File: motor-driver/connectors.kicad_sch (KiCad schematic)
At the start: 2 parts, among them J3 XT60PW-F, J4 B2B-PH-SM4-TB

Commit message: post revisions
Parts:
- added J1: USB_B_Micro, Connector_USB:USB_Micro-B_Amphenol_10103594-0001LF_Horizontal, symbol Connector:USB_B_Micro
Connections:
- net 5V: now also J1.1 (VBUS)
- net GND: now also J1.5 (GND), J1.6 (Shield)
- net 14V renamed V_BUS
- new net USB_D+: J1.3 (D+)
- new net USB_D-: J1.2 (D-)
- no-connect marks 1 -> 2
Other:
- note added: "Power Connections"
- note added: "RP MircoUSB"
- company: (none) -> Drone 
- moved on the sheet: J3, J4

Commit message: added spi connection
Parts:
- added J5: S4B-XH-A, S4B-XH-A:JST_S4B-XH-A, symbol S4B-XH-A:S4B-XH-A
- J1: value USB_B_Micro -> 10103594-0001LF
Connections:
- new net CS: J5.2
- new net MISO: J5.4
- new net MOSI: J5.1
- new net SCLK: J5.3
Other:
- note added: "SPI Connection"

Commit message: bom finished
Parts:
- J1: MANUFACTURER (none) -> Amphenol ICC (FCI); MPN (none) -> 10103594-0001LF; Supplier (none) -> Digikey
- J3: Availability In Stock -> (none); CREATOR KARTHIK -> (none); Check_prices https://www.snapeda.com/parts/XT60PW-F/AMASS/view-part/?ref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 -> (none); Description_1 Connector: DC supply; socket; female; XT60; 30A; 500V; PIN: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 -> (none); MPN (none) -> XT60PW-F
- J4: Availability In Stock -> (none); Check_prices https://www.snapeda.com/parts/B2B-PH-SM4-TB/JST/view-part/?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 -> (none); Description_1 Connector Header Surface Mount 2 position 0.079 (2.00mm) -> (none); MPN (none) -> B2B-PH-SM4-TB; Supplier (none) -> Digikey
- J5: Availability In Stock -> (none); Check_prices https://www.snapeda.com/parts/S4B-XH-A/JST/view-part/?ref=e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 -> (none); Description_1 Connector Header Through Hole, Right Angle 4 position 0.098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 -> (none); MPN (none) -> S4B-XH-A; Supplier (none) -> Digikey
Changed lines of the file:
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@@
+			)
+		)
+		(property "MPN" "10103594-0001LF"
+			(at 168.91 95.25 0)
+			(effects
+				(font
+					(size 1.27 1.27)
+				)
+				(hide yes)
+			)
+		)
+		(property "Supplier" "Digikey"
+			(at 168.91 95.25 0)
+			(effects
+				(font
+					(size 1.27 1.27)
+				)
+				(hide yes)
+			)
+		)
+		(property "MANUFACTURER" "Amphenol ICC (FCI)"
+			(at 168.91 95.25 0)
+			(effects
+				(font
+					(size 1.27 1.27)
+				)
+				(hide yes)
 			)
 		)
@@
 			)
 		)
-		(property "Check_prices" "https://www.snapeda.com/parts/B2B-PH-SM4-TB/JST/view-part/?ref=eda"
-			(at 119.38 113.03 0)
-			(effects
-				(font
-					(size 1.27 1.27)
-				)
-				(justify bottom)
-				(hide yes)
-			)
-		)
 		(property "STANDARD" "Manufacturer Recommendations"
 			(at 119.38 113.03 0)
@@
 			)
 		)
-		(property "Description_1" "Connector Header Surface Mount 2 position 0.079 (2.00mm)"
-			(at 119.38 113.03 0)
-			(effects
-				(font
-					(size 1.27 1.27)
-				)
-				(justify bottom)
-				(hide yes)
-			)
-		)
-		(property "Availability" "In Stock"
-			(at 119.38 113.03 0)
-			(effects
-				(font
-					(size 1.27 1.27)
-				)
-				(justify bottom)
-				(hide yes)
-			)
-		)
 		(property "MANUFACTURER" "JST"
 			(at 119.38 113.03 0)
@@
 				)
 				(justify bottom)
+				(hide yes)
+			)
+		)
+		(property "MPN" "B2B-PH-SM4-TB"
+			(at 119.38 113.03 0)
+			(effects
+				(font
+					(size 1.27 1.27)
+				)
+				(hide yes)
+			)
+		)
+		(property "Supplier" "Digikey"
+			(at 119.38 113.03 0)
+			(effects
+				(font
+					(size 1.27 1.27)
+				)
 				(hide yes)
 			)
@@
 			)
 		)
-		(property "CREATOR" "KARTHIK"
-			(at 123.19 93.98 0)
-			(effects
-				(font
-					(size 1.27 1.27)
-				)
-				(justify bottom)
-				(hide yes)
-			)
-		)
 		(property "Price" "None"
 			(at 123.19 93.98 0)
@@
 			)
 		)
-		(property "Check_prices" "https://www.snapeda.com/parts/XT60PW-F/AMASS/view-part/?ref=eda"
-			(at 123.19 93.98 0)
-			(effects
-				(font
-					(size 1.27 1.27)
-				)
-				(justify bottom)
-				(hide yes)
-			)
-		)
 		(property "STANDARD" "Manufacturer Recommendation"
 			(at 123.19 93.98 0)
@@
 			)
 		)
-		(property "Description_1" "Connector: DC supply; socket; female; XT60; 30A; 500V; PIN: 2; THT"
-			(at 123.19 93.98 0)
-			(effects
-				(font
-					(size 1.27 1.27)
-				)
-				(justify bottom)
-				(hide yes)
-			)
-		)
-		(property "Availability" "In Stock"
-			(at 123.19 93.98 0)
-			(effects
-				(font
-					(size 1.27 1.27)
-				)
-				(justify bottom)
-				(hide yes)
-			)
-		)
 		(property "MANUFACTURER" "AMASS"
 			(at 123.19 93.98 0)
@@
 				)
 				(justify bottom)
+				(hide yes)
+			)
+		)
+		(property "MPN" "XT60PW-F"
+			(at 123.19 93.98 0)
+			(effects
+				(font
+					(size 1.27 1.27)
+				)
+				(hide yes)
+			)
+		)
+		(property "Supplier" ""
+			(at 123.19 93.98 0)
+			(effects
+				(font
+					(size 1.27 1.27)
+				)
 				(hide yes)
 			)
@@
 			)
 		)
-		(property "Description_1" "Connector Header Through Hole, Right Angle 4 position 0.098 (2.50mm)"
-			(at 214.63 93.98 0)
-			(effects
-				(font
-					(size 1.27 1.27)
-				)
-				(justify bottom)
-				(hide yes)
-			)
-		)
 		(property "Package" "None"
 			(at 214.63 93.98 0)
@@
 			)
 		)
-		(property "Check_prices" "https://www.snapeda.com/parts/S4B-XH-A/JST/view-part/?ref=eda"
-			(at 214.63 93.98 0)
-			(effects
-				(font
-					(size 1.27 1.27)
-				)
-				(justify bottom)
-				(hide yes)
-			)
-		)
 		(property "SnapEDA_Link" "https://www.snapeda.com/parts/S4B-XH-A/JST/view-part/?ref=snap"
 			(at 214.63 93.98 0)
@@
 			)
 		)
-		(property "Availability" "In Stock"
-			(at 214.63 93.98 0)
-			(effects
-				(font
-					(size 1.27 1.27)
-				)
-				(justify bottom)
-				(hide yes)
-			)
-		)
 		(property "MANUFACTURER" "JST"
 			(at 214.63 93.98 0)
@@
 				(hide yes)
 			)
+		)
+		(property "MPN" "S4B-XH-A"
+			(at 214.63 93.98 0)
+			(effects
+				(font
+					(size 1.27 1.27)
+				)
+				(hide yes)
+			)
+		)
+		(property "Supplier" "Digikey"
+			(at 214.63 93.98 0)
+			(effects
+				(font
+					(size 1.27 1.27)
+				)
+				(hide yes)
+			)

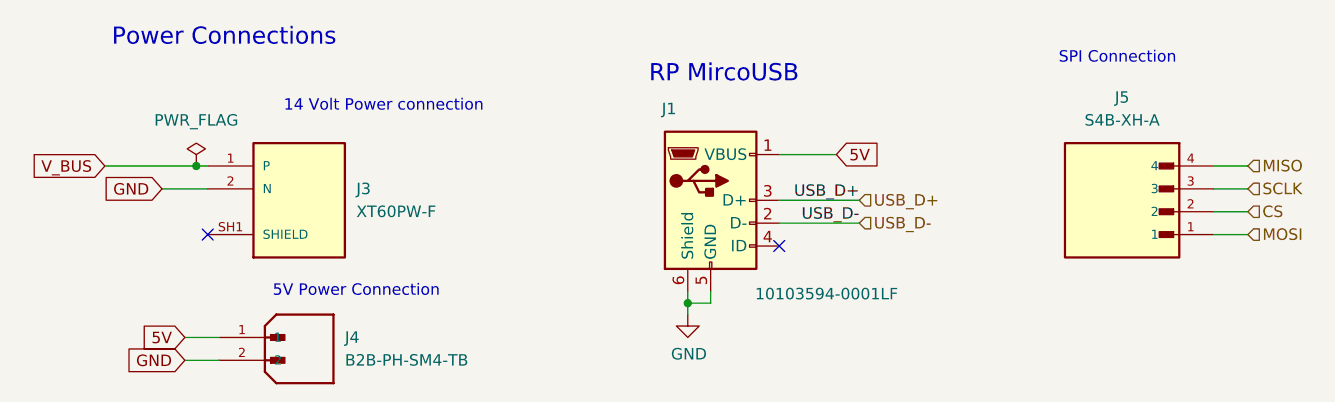
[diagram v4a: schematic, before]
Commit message: changed push buttons and zone clearances
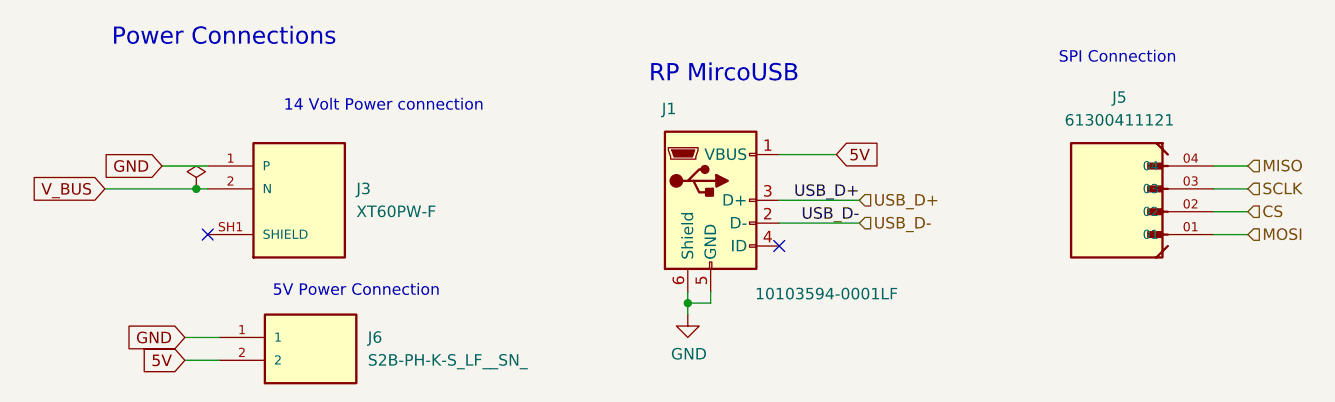
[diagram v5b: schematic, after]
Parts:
- removed J4: B2B-PH-SM4-TB, B2B-PH-SM4-TB:JST_B2B-PH-SM4-TB, symbol B2B-PH-SM4-TB:B2B-PH-SM4-TB
- removed J5: S4B-XH-A, S4B-XH-A:JST_S4B-XH-A, symbol S4B-XH-A:S4B-XH-A
- added J5: 61300411121, 61300411121:WURTH_61300411121, symbol 61300411121:61300411121
- added J6: S2B-PH-K-S_LF__SN_, S2B-PH-K:JST_S2B-PH-K-S_LF__SN_, symbol S2B-PH-K-S_LF__SN_:S2B-PH-K-S_LF__SN_
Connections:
- net 5V: now also J6.2
- net CS: now also J5.02
- net GND: now also J3.1 (P), J6.1; no longer J3.2 (N)
- net MISO: now also J5.04
- net MOSI: now also J5.01
- net SCLK: now also J5.03
- net V_BUS: now also J3.2 (N); no longer J3.1 (P)
